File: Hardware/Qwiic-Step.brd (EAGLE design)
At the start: 50.8 x 50.8 mm, 101 parts, among them J1 PTH, J2 Qwiic Right Angle, J3 5.5x2.1mm Barrel, J4 Qwiic Right Angle, J5 ISP, U1 A4988ALT1, U2 ATMEGA328P_TQFP, U4 HV7801, Y1 16MHz

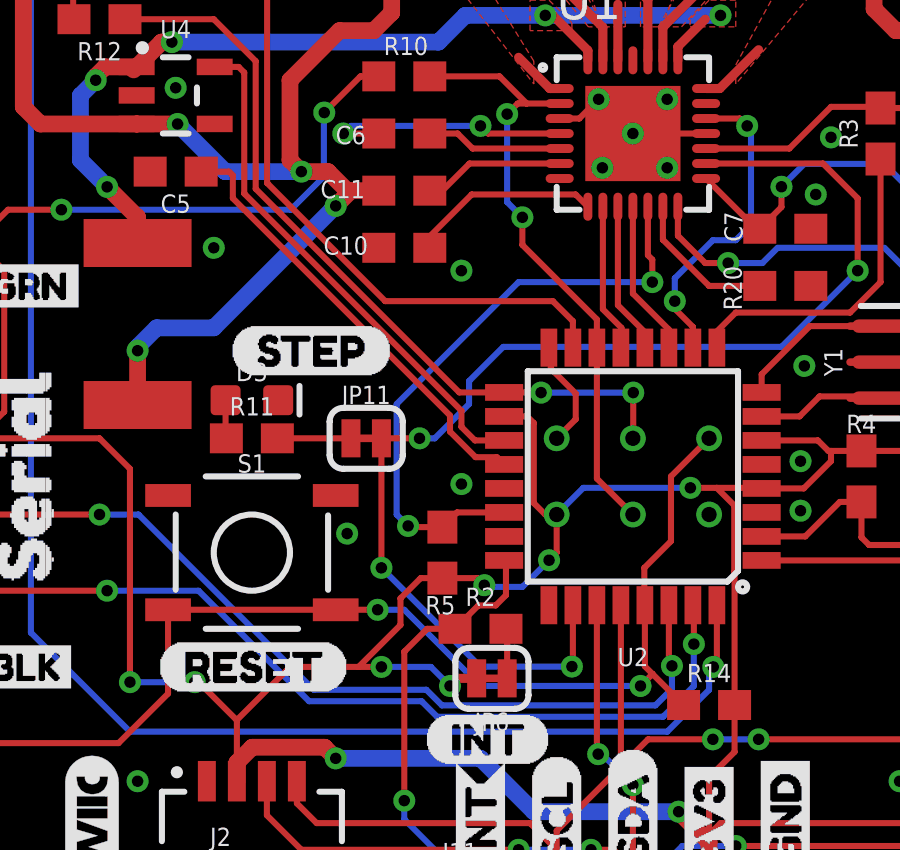
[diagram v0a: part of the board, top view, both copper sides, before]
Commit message: Superficial function name changes and board update
Rev 2 of Qwiic Step board! Fixed: MOSI was not connected to ISP pins! Adjusted MOSI and ADR jumper
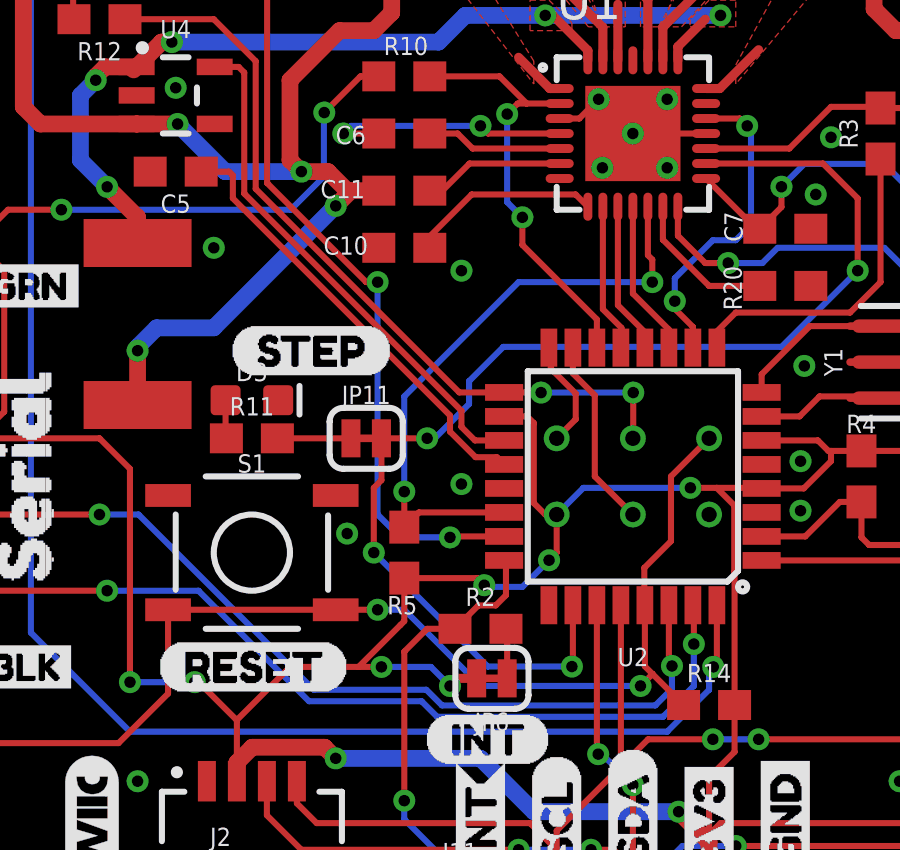
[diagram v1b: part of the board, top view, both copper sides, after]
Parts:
- moved R5 1.27 mm to (17.8, 12.7)
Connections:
- new net MOSI: J5.4, U2.15
- net !ENABLE!: no longer J5.4
- net ADR: now also U2.23; no longer U2.15
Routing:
- net MOSI: track 0.00 -> 6.39 mm
- net !ENABLE!: track 20.6 -> 14.5 mm
- net ADR: track 22.3 -> 26.6 mm, vias 0 -> 2
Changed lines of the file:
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@@
 <attribute name="VALUE" value="20k" x="32.3088" y="13.1572" size="0.6096" layer="27"/>
 </element>
-<element name="R5" library="SparkFun-Resistors" package="0603" value="20k" x="19.05" y="12.7" smashed="yes" rot="R270">
-<attribute name="NAME" x="19.4818" y="11.2522" size="0.6096" layer="25" rot="R180"/>
-<attribute name="PROD_ID" value="RES-09383" x="19.05" y="12.7" size="1.778" layer="27" rot="R270" display="off"/>
-<attribute name="VALUE" value="20k" x="19.7866" y="14.859" size="0.6096" layer="27" rot="R180"/>
+<element name="R5" library="SparkFun-Resistors" package="0603" value="20k" x="17.78" y="12.7" smashed="yes" rot="R270">
+<attribute name="NAME" x="18.2118" y="11.2522" size="0.6096" layer="25" rot="R180"/>
+<attribute name="PROD_ID" value="RES-09383" x="17.78" y="12.7" size="1.778" layer="27" rot="R270" display="off"/>
+<attribute name="VALUE" value="20k" x="18.5166" y="14.859" size="0.6096" layer="27" rot="R180"/>
 </element>
 <element name="R10" library="SparkFun-Resistors" package="0603" value="20k" x="17.78" y="28.575" smashed="yes" rot="R180">
@@
 <contactref element="R10" pad="1"/>
 <contactref element="U1" pad="2"/>
-<contactref element="J5" pad="4"/>
 <contactref element="U2" pad="14"/>
 <wire x1="22.96" y1="27.67" x2="21.86" y2="27.67" width="0.2032" layer="1"/>
 <wire x1="21.86" y1="27.67" x2="20.955" y2="28.575" width="0.2032" layer="1"/>
 <wire x1="20.955" y1="28.575" x2="18.63" y2="28.575" width="0.2032" layer="1"/>
-<wire x1="24.2" y1="19.5326" x2="24.2" y2="15.17" width="0.2032" layer="1"/>
-<wire x1="24.2" y1="15.17" x2="25.4" y2="13.97" width="0.2032" layer="1"/>
 <via x="21.209" y="27.3177" extent="1-16" drill="0.381"/>
 <wire x1="21.209" y1="27.3177" x2="21.209" y2="24.384" width="0.2032" layer="16"/>
@@
 <wire x1="23.368" y1="8.89" x2="23.368" y2="8.9027" width="0.2032" layer="1"/>
 <via x="23.368" y="8.9027" extent="1-16" drill="0.381"/>
-<wire x1="23.368" y1="8.9027" x2="20.3073" y2="8.9027" width="0.2032" layer="16"/>
-<wire x1="20.3073" y1="8.9027" x2="17.018" y2="12.192" width="0.2032" layer="16"/>
-<via x="17.018" y="12.192" extent="1-16" drill="0.381"/>
-<wire x1="17.018" y1="16.51" x2="18.288" y2="16.51" width="0.2032" layer="1"/>
-<via x="18.288" y="16.51" extent="1-16" drill="0.381"/>
-<wire x1="18.288" y1="16.51" x2="18.796" y2="16.51" width="0.2032" layer="16"/>
+<wire x1="23.368" y1="8.9027" x2="20.5613" y2="8.9027" width="0.2032" layer="16"/>
+<wire x1="20.5613" y1="8.9027" x2="16.764" y2="12.7" width="0.2032" layer="16"/>
+<via x="16.764" y="12.7" extent="1-16" drill="0.381"/>
+<wire x1="17.018" y1="16.51" x2="18.542" y2="16.51" width="0.2032" layer="1"/>
+<via x="18.542" y="16.51" extent="1-16" drill="0.381"/>
+<wire x1="18.542" y1="16.51" x2="18.796" y2="16.51" width="0.2032" layer="16"/>
 <wire x1="19.939" y1="17.653" x2="19.939" y2="18.415" width="0.2032" layer="16"/>
 <wire x1="19.939" y1="18.415" x2="21.082" y2="19.558" width="0.2032" layer="16"/>
@@
 <wire x1="21.082" y1="19.558" x2="30.353" y2="19.558" width="0.2032" layer="16"/>
 <wire x1="32.893" y1="24.511" x2="31.734" y2="25.67" width="0.2032" layer="1"/>
-<wire x1="17.018" y1="16.51" x2="17.018" y2="12.192" width="0.2032" layer="1"/>
+<wire x1="17.018" y1="16.51" x2="17.018" y2="15.113" width="0.2032" layer="1"/>
+<wire x1="17.018" y1="15.113" x2="16.764" y2="14.859" width="0.2032" layer="1"/>
+<wire x1="16.764" y1="14.859" x2="16.764" y2="12.7" width="0.2032" layer="1"/>
 </signal>
 <signal name="N$31">
@@
 <via x="20.447" y="11.6145" extent="1-16" drill="0.381"/>
 <wire x1="20.447" y1="11.6145" x2="20.2115" y2="11.85" width="0.2032" layer="1"/>
-<wire x1="20.2115" y1="11.85" x2="19.05" y2="11.85" width="0.2032" layer="1"/>
+<wire x1="20.2115" y1="11.85" x2="17.78" y2="11.85" width="0.2032" layer="1"/>
 <wire x1="21.1074" y1="17.24" x2="21.876" y2="17.24" width="0.2032" layer="1"/>
 <wire x1="21.876" y1="17.24" x2="22.098" y2="17.018" width="0.2032" layer="1"/>
@@
 <wire x1="22.098" y1="14.351" x2="22.479" y2="13.97" width="0.2032" layer="1"/>
 <wire x1="22.479" y1="13.97" x2="22.86" y2="13.97" width="0.2032" layer="1"/>
-<wire x1="18.327" y1="11.85" x2="19.05" y2="11.85" width="0.2032" layer="1"/>
-<wire x1="17.653" y1="11.176" x2="18.327" y2="11.85" width="0.2032" layer="1"/>
 <wire x1="37.6" y1="5.08" x2="37.6" y2="4.199" width="0.2032" layer="1"/>
 <wire x1="37.6" y1="4.199" x2="37.084" y2="3.683" width="0.2032" layer="1"/>
@@
 <wire x1="12.2" y1="7.12" x2="13.97" y2="8.89" width="0.2032" layer="1"/>
 <wire x1="13.97" y1="8.89" x2="16.256" y2="8.89" width="0.2032" layer="1"/>
-<wire x1="17.653" y1="11.176" x2="17.653" y2="10.287" width="0.2032" layer="1"/>
+<via x="17.018" y="8.89" extent="1-16" drill="0.381"/>
 <wire x1="17.653" y1="10.287" x2="16.256" y2="8.89" width="0.2032" layer="1"/>
-<via x="17.018" y="8.89" extent="1-16" drill="0.381"/>
 <wire x1="17.018" y1="8.89" x2="18.669" y2="8.89" width="0.2032" layer="16"/>
 <wire x1="18.669" y1="8.89" x2="19.304" y2="8.255" width="0.2032" layer="16"/>
@@
 <wire x1="20.193" y1="8.509" x2="19.558" y2="8.509" width="0.3048" layer="1"/>
 <wire x1="19.304" y1="8.255" x2="19.558" y2="8.509" width="0.3048" layer="1"/>
+<wire x1="17.653" y1="10.287" x2="17.78" y2="10.414" width="0.2032" layer="1"/>
+<wire x1="17.78" y1="10.414" x2="17.78" y2="11.85" width="0.2032" layer="1"/>
 </signal>
 <signal name="SCL">
@@
 <signal name="ADR">
 <contactref element="JP2" pad="2"/>
-<contactref element="U2" pad="15"/>
-<wire x1="23.4" y1="19.5326" x2="23.4" y2="20.415" width="0.2032" layer="1"/>
-<wire x1="22.733" y1="21.082" x2="17.145" y2="21.082" width="0.2032" layer="1"/>
-<wire x1="13.208" y1="25.019" x2="17.145" y2="21.082" width="0.2032" layer="1"/>
-<wire x1="23.4" y1="20.415" x2="22.733" y2="21.082" width="0.2032" layer="1"/>
 <wire x1="13.208" y1="34.29" x2="13.208" y2="25.019" width="0.2032" layer="1"/>
+<contactref element="U2" pad="23"/>
+<via x="16.891" y="21.717" extent="1-16" drill="0.381"/>
+<wire x1="16.51" y1="21.717" x2="16.891" y2="21.717" width="0.2032" layer="1"/>
+<wire x1="13.208" y1="25.019" x2="16.51" y2="21.717" width="0.2032" layer="1"/>
+<wire x1="16.891" y1="21.717" x2="16.891" y2="13.97" width="0.2032" layer="16"/>
+<wire x1="16.891" y1="13.97" x2="17.653" y2="13.208" width="0.2032" layer="16"/>
+<via x="19.304" y="13.208" extent="1-16" drill="0.381"/>
+<wire x1="19.304" y1="13.208" x2="19.336" y2="13.24" width="0.2032" layer="1"/>
+<wire x1="19.336" y1="13.24" x2="21.1074" y2="13.24" width="0.2032" layer="1"/>
+<wire x1="17.653" y1="13.208" x2="19.304" y2="13.208" width="0.2032" layer="16"/>
 </signal>
 <signal name="N$26">
@@
 <contactref element="R5" pad="1"/>
 <contactref element="U2" pad="22"/>
-<wire x1="19.05" y1="13.55" x2="19.54" y2="14.04" width="0.2032" layer="1"/>
-<wire x1="19.54" y1="14.04" x2="21.1074" y2="14.04" width="0.2032" layer="1"/>
-<wire x1="19.05" y1="13.55" x2="17.946" y2="13.55" width="0.2032" layer="1"/>
-<wire x1="17.946" y1="13.55" x2="17.907" y2="13.589" width="0.2032" layer="1"/>
-<via x="17.907" y="13.589" extent="1-16" drill="0.381"/>
-<wire x1="17.907" y1="13.589" x2="17.526" y2="13.97" width="0.2032" layer="16"/>
-<wire x1="17.526" y1="17.653" x2="21.59" y2="21.717" width="0.2032" layer="16"/>
-<wire x1="17.526" y1="13.97" x2="17.526" y2="17.653" width="0.2032" layer="16"/>
+<wire x1="17.78" y1="13.55" x2="18.27" y2="14.04" width="0.2032" layer="1"/>
+<wire x1="18.27" y1="14.04" x2="21.1074" y2="14.04" width="0.2032" layer="1"/>
+<wire x1="17.78" y1="13.55" x2="17.78" y2="14.732" width="0.2032" layer="1"/>
+<via x="17.78" y="14.732" extent="1-16" drill="0.381"/>
+<wire x1="17.78" y1="17.907" x2="21.59" y2="21.717" width="0.2032" layer="16"/>
+<wire x1="17.78" y1="14.732" x2="17.78" y2="17.907" width="0.2032" layer="16"/>
 <wire x1="26.0477" y1="21.717" x2="21.59" y2="21.717" width="0.2032" layer="16"/>
 <via x="26.0477" y="21.717" extent="1-16" drill="0.381"/>
@@
 <wire x1="6.985" y1="25.781" x2="7.874" y2="24.892" width="0.5588" layer="16"/>
 </signal>
+<signal name="MOSI">
+<contactref element="J5" pad="4"/>
+<contactref element="U2" pad="15"/>
+<wire x1="25.4" y1="13.97" x2="24.13" y2="15.24" width="0.2032" layer="1"/>
+<wire x1="23.4" y1="18.67335625" x2="23.4" y2="19.5326" width="0.2032" layer="1"/>
+<wire x1="24.13" y1="15.24" x2="24.13" y2="17.94335625" width="0.2032" layer="1"/>
+<wire x1="24.13" y1="17.94335625" x2="23.4" y2="18.67335625" width="0.2032" layer="1"/>
+</signal>
 </signals>

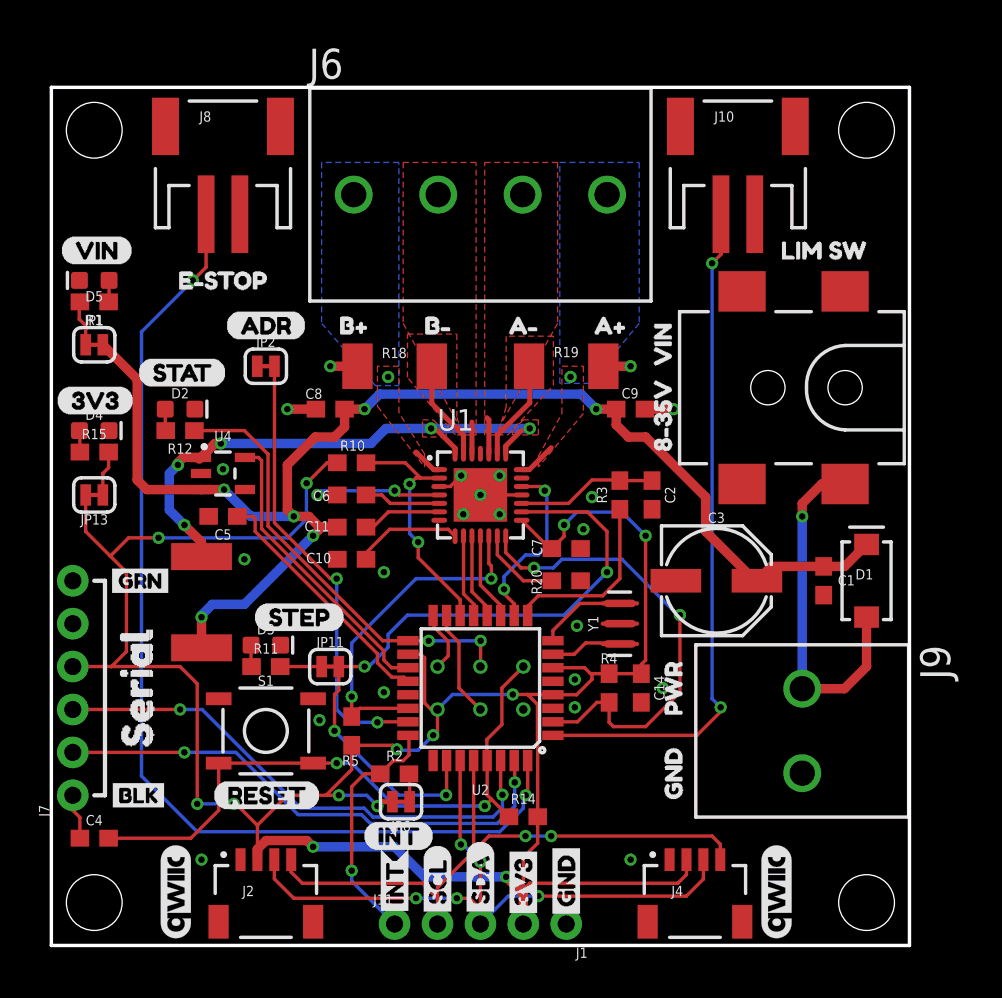
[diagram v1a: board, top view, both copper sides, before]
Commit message: Updated Qwiic Step board, working on examples for Rev 1 hardware
Updates to board:
Fixed serial programming pins
Moved ADR jumper to MOSI pin to free up GPIO
Moved A49885 reset pin to GPIO (from analog input pin)
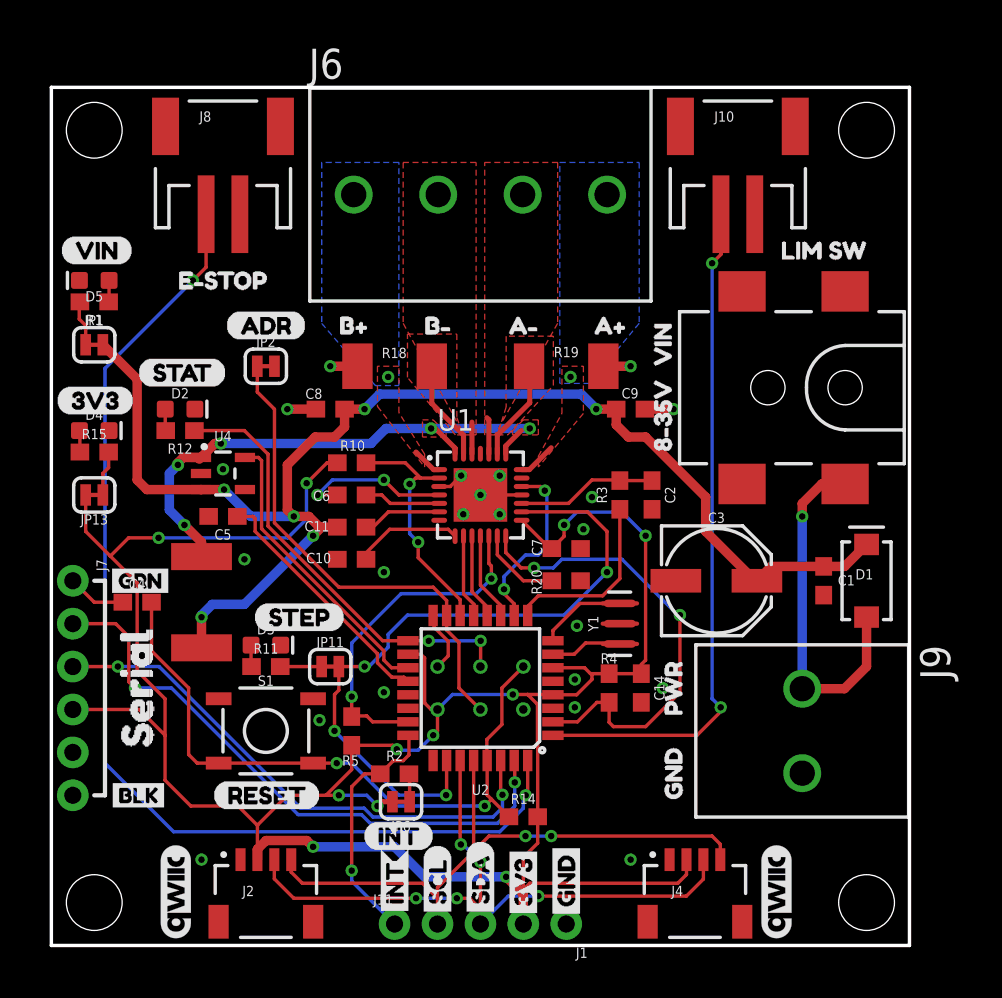
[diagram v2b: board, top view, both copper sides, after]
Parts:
- moved C4 14.2 mm to (5.08, 20.3)
- moved J7 12.7 mm to (1.27, 21.6), turned to 270 degrees
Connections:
- removed net ADR: JP2.2, U2.23
- net A49885_!RESET!: now also U2.23; no longer U2.22
- net GND: now also JP2.2; no longer JP2.1
- net MOSI: now also JP2.1
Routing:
- net ADR: track 26.6 -> 0.00 mm, vias 2 -> 0
- net MOSI: track 6.39 -> 29.1 mm
- net TXO: track 31.0 -> 35.8 mm
- net INT0: track 62.3 -> 64.9 mm
- net !RST!: track 37.7 -> 39.6 mm
- net RXI: track 31.1 -> 32.2 mm
- net 3.3V: track 152.7 -> 153.7 mm, vias 13 -> 11
- net DTR: track 2.71 -> 3.49 mm
- net N$8: track 8.60 -> 9.13 mm

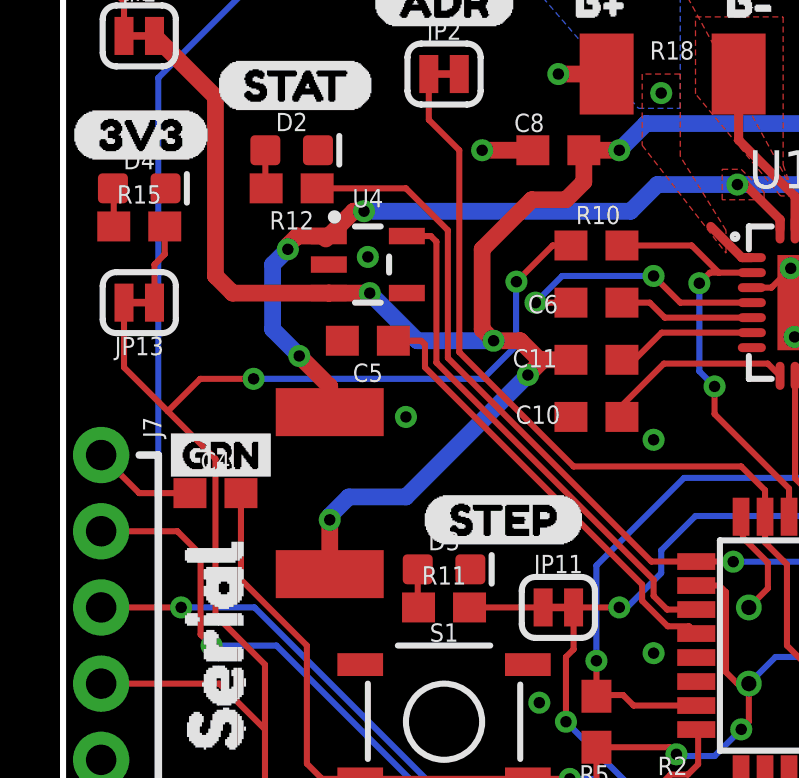
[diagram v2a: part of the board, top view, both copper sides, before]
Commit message: Removed current sense IC. Switched around ADC pins
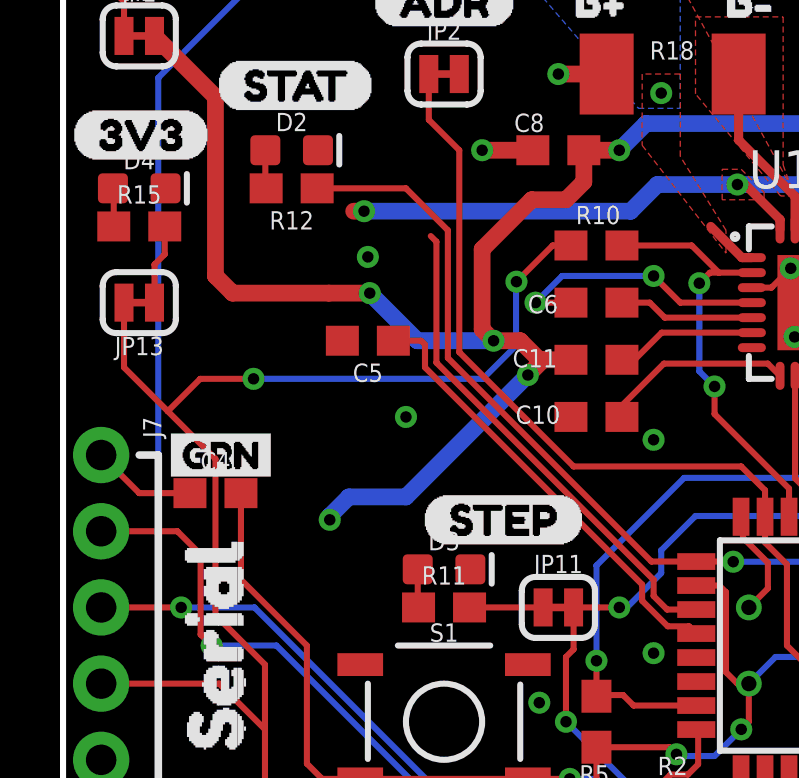
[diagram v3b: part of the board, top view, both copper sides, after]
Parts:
- removed R6: 0.25OHM_RES, qwiic_step:2512_RES
- removed U4: HV7801, SparkFun-IC-Special-Function:SOT23-5
- JP2: value INT -> ADR
- R11: value 1k -> 470
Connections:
- removed net CURR_SENSE: U2.19, U4.5
- removed net EP: U2.25
- removed net MOTOR_SUPPLY: R6.2, U1.22, U1.28, U4.1
- removed net N$32: R19.2, U1.23
- new net CURRENT_SENSE: R19.2, U1.23, U2.19
- net GND: no longer U4.4
- net VIN: now also U1.22, U1.28; no longer R6.1, U4.3
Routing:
- net MOTOR_SUPPLY: track 32.3 -> 0.00 mm, vias 5 -> 0
- net CURRENT_SENSE: track 0.00 -> 22.7 mm
- net VIN: track 80.6 -> 101.7 mm, vias 6 -> 9
- net CURR_SENSE: track 17.5 -> 0.00 mm
- net N$32: track 5.99 -> 0.00 mm
- added copper zone on layer 1, net CURRENT_SENSE
- removed copper zone on layer 1, net N$32
